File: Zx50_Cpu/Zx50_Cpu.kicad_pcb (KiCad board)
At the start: 2 copper layers, 135.9 x 100.4 mm, 25 parts, among them J1 Zx50_EdgeConnector, J2 Conn_02x05_Odd_Even, J2 FrontPanelConnect, J3 Clock Mezzanine, J4 Front Panel, SW1 RESET, U1 74AHC1G14, U2 SN74AHCT245N, U3 SN74AHCT245N, U4 Z84C00xxP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

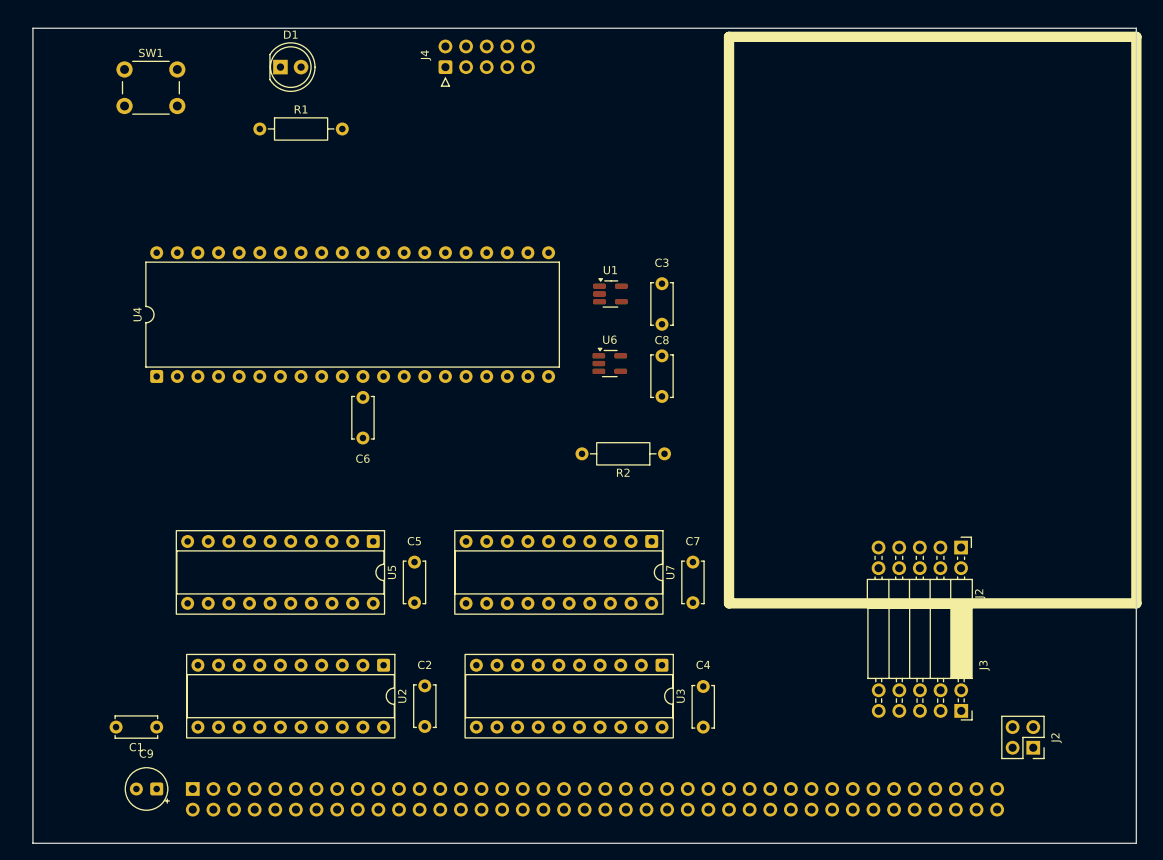
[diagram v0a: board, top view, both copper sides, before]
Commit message: add ground plane
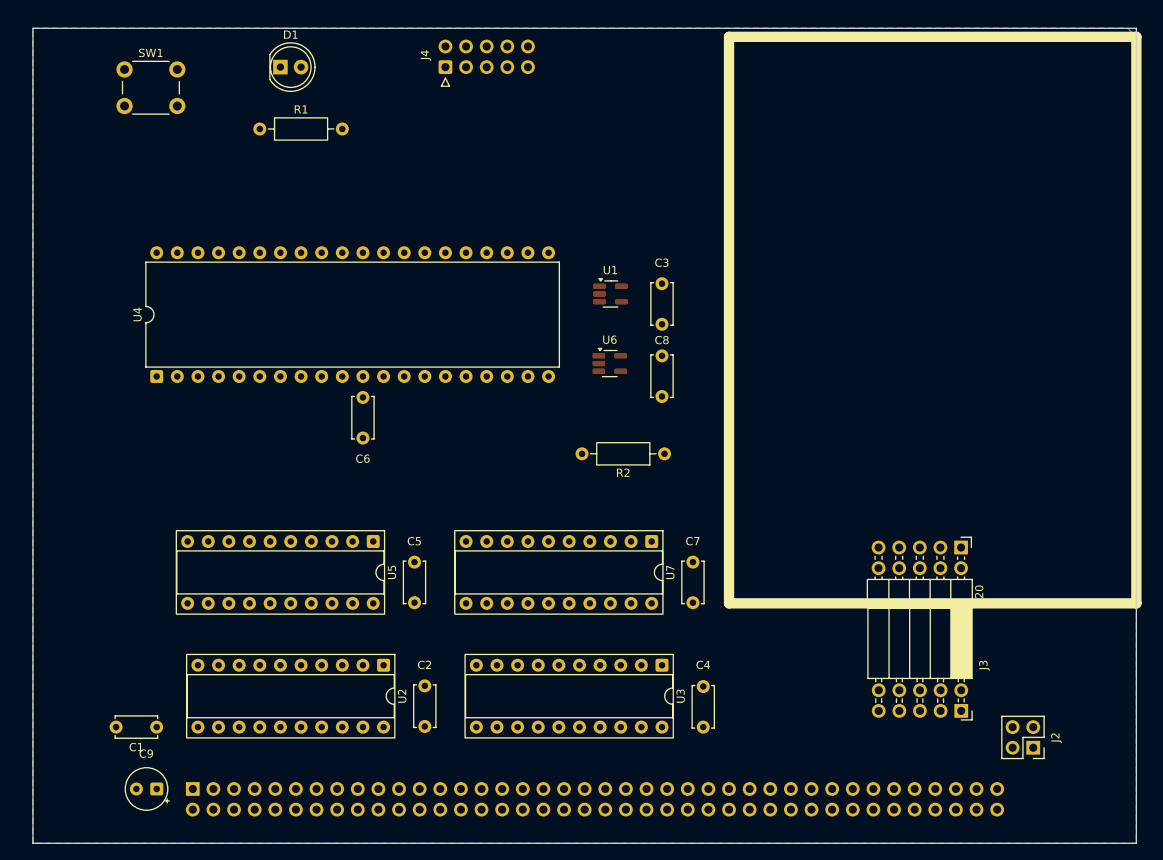
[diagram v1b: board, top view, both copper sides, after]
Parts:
- renumbered J2 to J20
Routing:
- added copper zone on B.Cu, net GND
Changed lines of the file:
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@@
 	)
 	(footprint "zx50_footprints:PinHeader_2x05_P2.54mm_Horizontal_Edge"
+		(locked yes)
 		(layer "F.Cu")
 		(at 135.89 127.745 -90)
 		(descr "Through hole angled pin header, 2x05, 2.54mm pitch, 6mm pin length, double rows")
 		(tags "Through hole angled pin header THT 2x05 2.54mm double row")
-		(property "Reference" "J2"
-			(at 5.655 -2.27 270)
+		(property "Reference" "J20"
+			(at 5.655 -2.27 90)
 			(layer "F.SilkS")
 			(effects
@@
 		)
 		(property "Datasheet" "~"
-			(at 0 0 270)
+			(at 0 0 90)
 			(layer "F.Fab")
 			(hide yes)
@@
 		)
 		(property "Description" "Generic connector, double row, 02x05, odd/even pin numbering scheme (row 1 odd numbers, row 2 even numbers), script generated (kicad-library-utils/schlib/autogen/connector/)"
-			(at 0 0 270)
+			(at 0 0 90)
 			(layer "F.Fab")
 			(hide yes)
@@
 		)
 		(fill no)
+		(locked yes)
 		(layer "F.SilkS")
 	)
@@
 		(layer "Edge.Cuts")
 	)
-	(group ""
+	(zone
+		(net 2)
+		(net_name "GND")
+		(layer "B.Cu")
+		(hatch edge 0.5)
+		(connect_pads
+			(clearance 0.5)
+		)
+		(min_thickness 0.25)
+		(filled_areas_thickness no)
+		(fill yes
+			(thermal_gap 0.5)
+			(thermal_bridge_width 0.5)
+		)
+		(polygon
+			(pts
+				(xy 157.48 164.17) (xy 21.59 164.17) (xy 21.59 63.796001) (xy 156.425 63.796001) (xy 157.48 64.851001)
+			)
+		)
+	)
+	(group "ClockMez"
+		(locked yes)
 		(members "df25c40a-6a12-448e-8407-7a74b19934e7" "f29315db-56e4-487d-93fb-455f942f33dc")
 	)

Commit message: 4 layer done
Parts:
- removed J20: Conn_02x05_Odd_Even, zx50_footprints:PinHeader_2x05_P2.54mm_Horizontal_Edge
- R2: footprint Resistor_THT:R_Axial_DIN0207_L6.3mm_D2.5mm_P10.16mm_Horizontal -> Resistor_THT:R_Axial_DIN0207_L6.3mm_D2.5mm_P5.08mm_Vertical
- moved R2 28.3 mm to (71.1, 115.6), turned to -90 degrees
- moved C3 9.16 mm to (94.0, 87.6)
- moved U1 8.52 mm to (88.9, 88.9)
- moved C5 7.65 mm to (61.0, 135.3), turned to 0 degrees
- moved C7 6.84 mm to (96.5, 132.0)
- moved R1 6.84 mm to (43.2, 73.7)
- moved C6 6.38 mm to (58.4, 104.1)
- moved U4 6.35 mm to (33.0, 101.6)
- moved SW1 5.90 mm to (27.0, 68.6)
- moved U7 5.68 mm to (92.7, 124.5)
- moved C2 5.12 mm to (65.4, 147.2)
- moved C4 4.58 mm to (100.3, 147.3)
- moved C1 4.52 mm to (34.0, 153.4), turned to 90 degrees
- moved U3 3.59 mm to (96.5, 139.7)
- moved U2 3.59 mm to (62.2, 139.7)
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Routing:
- net GND: track 0.00 -> 384.8 mm, vias 0 -> 89
- net /CLK: track 0.00 -> 181.7 mm
- net /~STEP: track 0.00 -> 145.5 mm, vias 0 -> 1
- net /RUN: track 0.00 -> 145.5 mm, vias 0 -> 1
- net /~BUSRQ~: track 0.00 -> 118.4 mm, vias 0 -> 1
- net /~BUSAK~: track 0.00 -> 110.7 mm, vias 0 -> 1
- net /BUSAK: track 0.00 -> 109.3 mm, vias 0 -> 1
- net /A10: track 0.00 -> 100.9 mm, vias 0 -> 1
- net /~INT~: track 0.00 -> 100.9 mm, vias 0 -> 1
- net /~RESET_SW: track 0.00 -> 100.5 mm, vias 0 -> 1
- net /~WAIT~: track 0.00 -> 98.6 mm, vias 0 -> 1
- net /~RESET~: track 0.00 -> 95.7 mm, vias 0 -> 2
- net /A8: track 0.00 -> 89.6 mm, vias 0 -> 1
- net /A9: track 0.00 -> 89.5 mm, vias 0 -> 1
- net /A14: track 0.00 -> 83.1 mm, vias 0 -> 1
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- added copper zone on F.Cu, net +5V
- added copper zone on In2.Cu, net +5V
- added copper zone on In1.Cu, net GND
- removed copper zone on B.Cu, net GND
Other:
- board size 135.9 x 100.4 mm -> 139.2 x 100.3 mm
- copper layers 2 -> 4
- board text added: "BUS CONNECT"
- board text added: "CLOCK MEZZANINE"
- board text added: "POWER"
- board text added: "RESET"
- board text added: "RUN"
- board text added: "STEP"
